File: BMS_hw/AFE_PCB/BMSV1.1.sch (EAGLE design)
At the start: 287 parts, among them IC1 MC33771BEP, IC10 TLP152-COUPLERTOSHIBA, IC11 TLP152-COUPLERTOSHIBA, IC2 SFH6156-1, IC3 MIC28515V1, IC7 SFH6156-1, IC8 SFH6156-1, IC9 TLP152-COUPLERTOSHIBA, Q1 IRLML5203, Q2 BSS138PW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

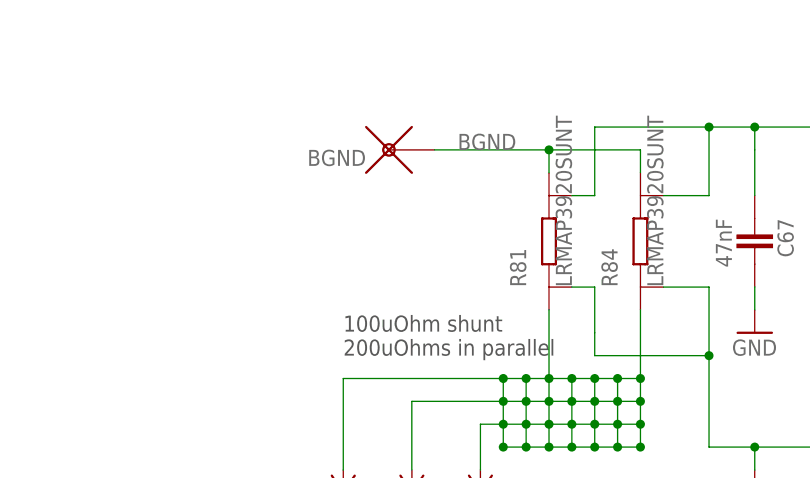
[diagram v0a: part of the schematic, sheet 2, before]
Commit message: 4.04mm space released from componrnrts for slidding!
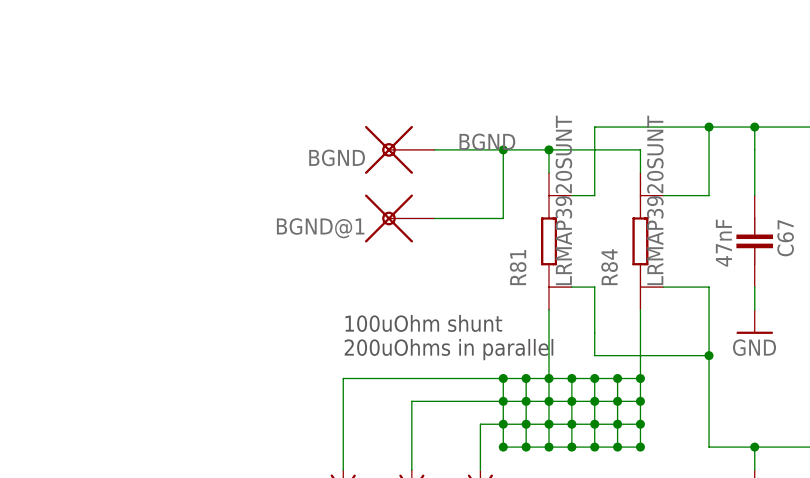
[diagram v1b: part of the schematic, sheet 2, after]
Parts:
- added BGND@1: (no value), simpa:WPAD
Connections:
- net BGND: now also BGND@1.P$1
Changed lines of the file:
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@@
 <part name="IC11" library="GreenFuel" deviceset="TLP152-COUPLER" device="TOSHIBA"/>
 <part name="R119" library="ipc-7351-resistor" deviceset="RESISTOR_" device="0402" value="127E"/>
+<part name="BGND@1" library="simpa" deviceset="WPAD" device=""/>
 </parts>
 <sheets>
@@
 <attribute name="VALUE" x="340.36" y="146.558" size="1.778" layer="96"/>
 </instance>
+<instance part="BGND@1" gate="G$1" x="261.62" y="231.14" smashed="yes" rot="R180">
+<attribute name="NAME" x="259.08" y="231.14" size="1.778" layer="95" font="vector" ratio="18" rot="R180"/>
+</instance>
 </instances>
 <busses>
@@
 <wire x1="279.4" y1="236.22" x2="279.4" y2="238.76" width="0.1524" layer="91"/>
 <wire x1="279.4" y1="238.76" x2="289.56" y2="238.76" width="0.1524" layer="91"/>
-<wire x1="279.4" y1="238.76" x2="266.7" y2="238.76" width="0.1524" layer="91"/>
+<wire x1="279.4" y1="238.76" x2="274.32" y2="238.76" width="0.1524" layer="91"/>
 <junction x="279.4" y="238.76"/>
 <label x="269.24" y="238.76" size="1.778" layer="95"/>
 <pinref part="BGND" gate="G$1" pin="P$1"/>
+<pinref part="BGND@1" gate="G$1" pin="P$1"/>
+<wire x1="274.32" y1="238.76" x2="266.7" y2="238.76" width="0.1524" layer="91"/>
+<wire x1="266.7" y1="231.14" x2="274.32" y2="231.14" width="0.1524" layer="91"/>
+<wire x1="274.32" y1="238.76" x2="274.32" y2="231.14" width="0.1524" layer="91"/>
+<junction x="274.32" y="238.76"/>
 </segment>
 <segment>

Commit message: last
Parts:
- removed BGND@1: (no value), simpa:WPAD
- added +12V, +3.3V, +5V, GND, GND@1, WAKE: TP-SMD60, simpa:TP-SMD60
- C69, C70, C81, C82: device ipc-7351-capacitor:CAPACITOR_0402 -> ipc-7351-capacitor:CAPACITOR_0805
- C74: value 47nF -> 1uF 100V; device ipc-7351-capacitor:CAPACITOR_0603 -> ipc-7351-capacitor:CAPACITOR_0805
- R79: value 2E -> 2.2E
- R98: value 300E -> 330E
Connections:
- net +12V: now also +12V.P$1
- net 3.3V: now also +3.3V.P$1
- net 5V: now also +5V.P$1
- net BGND: no longer BGND@1.P$1
- net GND: now also GND.P$1, GND@1.P$1
- net WAKE: now also WAKE.P$1
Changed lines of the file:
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@@
 <setting verticaltext="up"/>
 </settings>
-<grid distance="0.1" unitdist="inch" unit="mil" style="dots" multiple="1" display="yes" altdistance="0.01" altunitdist="inch" altunit="mil"/>
+<grid distance="0.1" unitdist="inch" unit="inch" style="lines" multiple="1" display="no" altdistance="0.01" altunitdist="inch" altunit="inch"/>
 <layers>
 <layer number="1" name="Top" color="4" fill="1" visible="no" active="no"/>
@@
 <part name="P+1" library="supply1" library_urn="urn:adsk.eagle:library:371" deviceset="VCC" device="" value="+12V"/>
 <part name="GND57" library="supply1" library_urn="urn:adsk.eagle:library:371" deviceset="GND" device=""/>
-<part name="C74" library="ipc-7351-capacitor" deviceset="CAPACITOR_" device="0603" value="47nF"/>
+<part name="C74" library="ipc-7351-capacitor" deviceset="CAPACITOR_" device="0805" value="1uF 100V"/>
 <part name="GND67" library="supply1" library_urn="urn:adsk.eagle:library:371" deviceset="GND" device=""/>
-<part name="R79" library="ipc-7351-resistor" deviceset="RESISTOR_" device="0603" value="2E"/>
+<part name="R79" library="ipc-7351-resistor" deviceset="RESISTOR_" device="0603" value="2.2E"/>
 <part name="GND66" library="supply1" library_urn="urn:adsk.eagle:library:371" deviceset="GND" device=""/>
 <part name="FRAME3" library="frames" library_urn="urn:adsk.eagle:library:229" deviceset="A3L-LOC" device=""/>
@@
 <part name="SUPPLY12" library="supply2" library_urn="urn:adsk.eagle:library:372" deviceset="GND" device=""/>
 <part name="Q2" library="simpa" deviceset="BSS138" device="PW"/>
-<part name="R98" library="ipc-7351-resistor" deviceset="RESISTOR_" device="0402" value="300E"/>
+<part name="R98" library="ipc-7351-resistor" deviceset="RESISTOR_" device="0402" value="330E"/>
 <part name="R3" library="ipc-7351-resistor" deviceset="RESISTOR_" device="0402" value="0E"/>
 <part name="R1" library="ipc-7351-resistor" deviceset="RESISTOR_" device="0402" value="0E"/>
@@
 <part name="U1" library="GreenFuel" deviceset="NCP1117LP" device="-PG"/>
 <part name="GND81" library="supply1" library_urn="urn:adsk.eagle:library:371" deviceset="GND" device=""/>
-<part name="C69" library="ipc-7351-capacitor" deviceset="CAPACITOR_" device="0402" value="10uF"/>
-<part name="C70" library="ipc-7351-capacitor" deviceset="CAPACITOR_" device="0402" value="10uF"/>
+<part name="C69" library="ipc-7351-capacitor" deviceset="CAPACITOR_" device="0805" value="10uF"/>
+<part name="C70" library="ipc-7351-capacitor" deviceset="CAPACITOR_" device="0805" value="10uF"/>
 <part name="GND82" library="supply1" library_urn="urn:adsk.eagle:library:371" deviceset="GND" device=""/>
 <part name="GND83" library="supply1" library_urn="urn:adsk.eagle:library:371" deviceset="GND" device=""/>
 <part name="U2" library="GreenFuel" deviceset="NCP1117LP" device="-PG"/>
 <part name="GND84" library="supply1" library_urn="urn:adsk.eagle:library:371" deviceset="GND" device=""/>
-<part name="C81" library="ipc-7351-capacitor" deviceset="CAPACITOR_" device="0402" value="10uF"/>
-<part name="C82" library="ipc-7351-capacitor" deviceset="CAPACITOR_" device="0402" value="10uF"/>
+<part name="C81" library="ipc-7351-capacitor" deviceset="CAPACITOR_" device="0805" value="10uF"/>
+<part name="C82" library="ipc-7351-capacitor" deviceset="CAPACITOR_" device="0805" value="10uF"/>
 <part name="GND85" library="supply1" library_urn="urn:adsk.eagle:library:371" deviceset="GND" device=""/>
 <part name="GND86" library="supply1" library_urn="urn:adsk.eagle:library:371" deviceset="GND" device=""/>
@@
 <part name="IC11" library="GreenFuel" deviceset="TLP152-COUPLER" device="TOSHIBA"/>
 <part name="R119" library="ipc-7351-resistor" deviceset="RESISTOR_" device="0402" value="127E"/>
-<part name="BGND@1" library="simpa" deviceset="WPAD" device=""/>
+<part name="+5V" library="simpa" deviceset="TP" device="-SMD60"/>
+<part name="GND" library="simpa" deviceset="TP" device="-SMD60"/>
+<part name="WAKE" library="simpa" deviceset="TP" device="-SMD60"/>
+<part name="+3.3V" library="simpa" deviceset="TP" device="-SMD60"/>
+<part name="+12V" library="simpa" deviceset="TP" device="-SMD60"/>
+<part name="GND@1" library="simpa" deviceset="TP" device="-SMD60"/>
 </parts>
 <sheets>
@@
 <attribute name="VALUE" x="340.36" y="146.558" size="1.778" layer="96"/>
 </instance>
-<instance part="BGND@1" gate="G$1" x="261.62" y="231.14" smashed="yes" rot="R180">
-<attribute name="NAME" x="259.08" y="231.14" size="1.778" layer="95" font="vector" ratio="18" rot="R180"/>
+<instance part="+12V" gate="G$1" x="302.26" y="68.58" smashed="yes" rot="R270">
+<attribute name="NAME" x="301.625" y="67.31" size="1.016" layer="95" font="vector" ratio="12" rot="R270"/>
+</instance>
+<instance part="GND@1" gate="G$1" x="325.12" y="71.12" smashed="yes">
+<attribute name="NAME" x="326.39" y="70.485" size="1.016" layer="95" font="vector" ratio="12"/>
 </instance>
 </instances>
@@
 <wire x1="317.5" y1="96.52" x2="317.5" y2="88.9" width="0.1524" layer="91"/>
 <wire x1="317.5" y1="88.9" x2="317.5" y2="81.28" width="0.1524" layer="91"/>
-<wire x1="317.5" y1="81.28" x2="317.5" y2="66.04" width="0.1524" layer="91"/>
+<wire x1="317.5" y1="81.28" x2="317.5" y2="71.12" width="0.1524" layer="91"/>
+<wire x1="317.5" y1="71.12" x2="317.5" y2="66.04" width="0.1524" layer="91"/>
 <wire x1="314.96" y1="96.52" x2="317.5" y2="96.52" width="0.1524" layer="91"/>
 <junction x="317.5" y="96.52"/>
@@
 <pinref part="C87" gate="G$1" pin="1"/>
 <wire x1="314.96" y1="114.3" x2="317.5" y2="114.3" width="0.1524" layer="91"/>
+<pinref part="GND@1" gate="G$1" pin="P$1"/>
+<wire x1="322.58" y1="71.12" x2="317.5" y2="71.12" width="0.1524" layer="91"/>
+<junction x="317.5" y="71.12"/>
 </segment>
 <segment>
@@
 <wire x1="279.4" y1="236.22" x2="279.4" y2="238.76" width="0.1524" layer="91"/>
 <wire x1="279.4" y1="238.76" x2="289.56" y2="238.76" width="0.1524" layer="91"/>
-<wire x1="279.4" y1="238.76" x2="274.32" y2="238.76" width="0.1524" layer="91"/>
 <junction x="279.4" y="238.76"/>
 <label x="269.24" y="238.76" size="1.778" layer="95"/>
 <pinref part="BGND" gate="G$1" pin="P$1"/>
-<pinref part="BGND@1" gate="G$1" pin="P$1"/>
-<wire x1="274.32" y1="238.76" x2="266.7" y2="238.76" width="0.1524" layer="91"/>
-<wire x1="266.7" y1="231.14" x2="274.32" y2="231.14" width="0.1524" layer="91"/>
-<wire x1="274.32" y1="238.76" x2="274.32" y2="231.14" width="0.1524" layer="91"/>
-<junction x="274.32" y="238.76"/>
+<wire x1="279.4" y1="238.76" x2="266.7" y2="238.76" width="0.1524" layer="91"/>
 </segment>
 <segment>
@@
 <wire x1="292.1" y1="106.68" x2="302.26" y2="106.68" width="0.1524" layer="91"/>
 <junction x="302.26" y="106.68"/>
+<pinref part="+12V" gate="G$1" pin="P$1"/>
+<wire x1="302.26" y1="71.12" x2="302.26" y2="81.28" width="0.1524" layer="91"/>
 </segment>
 </net>
@@
 <attribute name="VALUE" x="203.2" y="185.42" size="1.27" layer="96" font="vector" ratio="12"/>
 </instance>
+<instance part="+5V" gate="G$1" x="86.36" y="111.76" smashed="yes">
+<attribute name="NAME" x="87.63" y="111.125" size="1.016" layer="95" font="vector" ratio="12"/>
+</instance>
+<instance part="GND" gate="G$1" x="86.36" y="106.68" smashed="yes">
+<attribute name="NAME" x="87.63" y="106.045" size="1.016" layer="95" font="vector" ratio="12"/>
+</instance>
+<instance part="WAKE" gate="G$1" x="86.36" y="119.38" smashed="yes">
+<attribute name="NAME" x="87.63" y="118.745" size="1.016" layer="95" font="vector" ratio="12"/>
+</instance>
+<instance part="+3.3V" gate="G$1" x="38.1" y="93.98" smashed="yes" rot="R180">
+<attribute name="NAME" x="36.83" y="94.615" size="1.016" layer="95" font="vector" ratio="12" rot="R180"/>
+</instance>
 </instances>
 <busses>
@@
 <segment>
 <pinref part="JP6" gate="A" pin="8"/>
-<wire x1="68.58" y1="106.68" x2="73.66" y2="106.68" width="0.1524" layer="91"/>
 <label x="73.66" y="106.68" size="1.778" layer="95"/>
+<pinref part="GND" gate="G$1" pin="P$1"/>
+<wire x1="83.82" y1="106.68" x2="68.58" y2="106.68" width="0.1524" layer="91"/>
 </segment>
 <segment>
@@
 <segment>
 <pinref part="JP4" gate="A" pin="13"/>
-<wire x1="55.88" y1="93.98" x2="50.8" y2="93.98" width="0.1524" layer="91"/>
 <label x="45.72" y="93.98" size="1.778" layer="95"/>
+<pinref part="+3.3V" gate="G$1" pin="P$1"/>
+<wire x1="40.64" y1="93.98" x2="55.88" y2="93.98" width="0.1524" layer="91"/>
 </segment>
 <segment>
@@
 <segment>
 <pinref part="JP6" gate="A" pin="13"/>
-<wire x1="68.58" y1="119.38" x2="73.66" y2="119.38" width="0.1524" layer="91"/>
 <label x="73.66" y="119.38" size="1.778" layer="95" font="vector" ratio="12"/>
+<pinref part="WAKE" gate="G$1" pin="P$1"/>
+<wire x1="83.82" y1="119.38" x2="68.58" y2="119.38" width="0.1524" layer="91"/>
 </segment>
 </net>
@@
 <segment>
 <pinref part="JP6" gate="A" pin="10"/>
-<wire x1="68.58" y1="111.76" x2="73.66" y2="111.76" width="0.1524" layer="91"/>
 <label x="73.66" y="111.76" size="1.778" layer="95"/>
+<pinref part="+5V" gate="G$1" pin="P$1"/>
+<wire x1="83.82" y1="111.76" x2="68.58" y2="111.76" width="0.1524" layer="91"/>
 </segment>
 </net>

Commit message: board schematic and part updated
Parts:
- added R120: 1K, ipc-7351-resistor:RESISTOR_2010
- C75: device ipc-7351-capacitor:CAPACITOR_0402 -> ipc-7351-capacitor:CAPACITOR_0805
- Q2: value BSS138PW -> SI2392ADS-T1-GE3; device simpa:BSS138PW -> GreenFuel:BSS138
- R100, R99: device ipc-7351-resistor:RESISTOR_0402 -> ipc-7351-resistor:RESISTOR_0603
- R101, R102, R116, R117: value 33E -> 75E
- R103, R104: value 330E -> 75E
- R111, R112, R113, R114, R115, R80: value 330E -> 1K
- R86: value 380E -> 526E; device ipc-7351-resistor:RESISTOR_0402 -> ipc-7351-resistor:RESISTOR_0603
- R98: value 330E -> 1K; device ipc-7351-resistor:RESISTOR_0402 -> ipc-7351-resistor:RESISTOR_2010
- U1: value NCP1117LP-PG -> NCV1117ST33T3G
- U2: value NCP1117LP-PG -> NCV1117ST50T3G
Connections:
- net +12V: now also LED1.A, LED2.A, LED3.A, LED4.A
- net 3.3V: no longer LED1.A, LED2.A, LED3.A, LED4.A
- net BGND: now also R120.1
- net N$28: now also R120.2
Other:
- moved on the sheet: LED1, R98

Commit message: sch board updated
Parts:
- removed R120: 1K, ipc-7351-resistor:RESISTOR_2010
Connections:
- net BGND: no longer R120.1
- net N$28: no longer R120.2
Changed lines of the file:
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@@
 <part name="+12V" library="simpa" deviceset="TP" device="-SMD60"/>
 <part name="GND@1" library="simpa" deviceset="TP" device="-SMD60"/>
-<part name="R120" library="ipc-7351-resistor" deviceset="RESISTOR_" device="2010" value="1K"/>
 </parts>
 <sheets>
@@
 <attribute name="NAME" x="36.83" y="94.615" size="1.016" layer="95" font="vector" ratio="12" rot="R180"/>
 </instance>
-<instance part="R120" gate="G$1" x="226.06" y="231.14" smashed="yes" rot="R180">
-<attribute name="NAME" x="228.6" y="229.616" size="1.778" layer="95" rot="R180"/>
-<attribute name="VALUE" x="228.6" y="234.442" size="1.778" layer="96" rot="R180"/>
-</instance>
 </instances>
 <busses>
@@
 <pinref part="R98" gate="G$1" pin="1"/>
 <label x="233.68" y="223.52" size="1.778" layer="95"/>
-<pinref part="R120" gate="G$1" pin="1"/>
-<wire x1="231.14" y1="231.14" x2="233.68" y2="231.14" width="0.1524" layer="91"/>
 <wire x1="233.68" y1="231.14" x2="233.68" y2="218.44" width="0.1524" layer="91"/>
 </segment>
@@
 <wire x1="218.44" y1="223.52" x2="218.44" y2="218.44" width="0.1524" layer="91"/>
 <wire x1="218.44" y1="218.44" x2="223.52" y2="218.44" width="0.1524" layer="91"/>
-<wire x1="218.44" y1="223.52" x2="218.44" y2="231.14" width="0.1524" layer="91"/>
-<junction x="218.44" y="223.52"/>
-<pinref part="R120" gate="G$1" pin="2"/>
-<wire x1="218.44" y1="231.14" x2="220.98" y2="231.14" width="0.1524" layer="91"/>
 </segment>
 </net>
